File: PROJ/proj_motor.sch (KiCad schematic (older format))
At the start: 12 parts

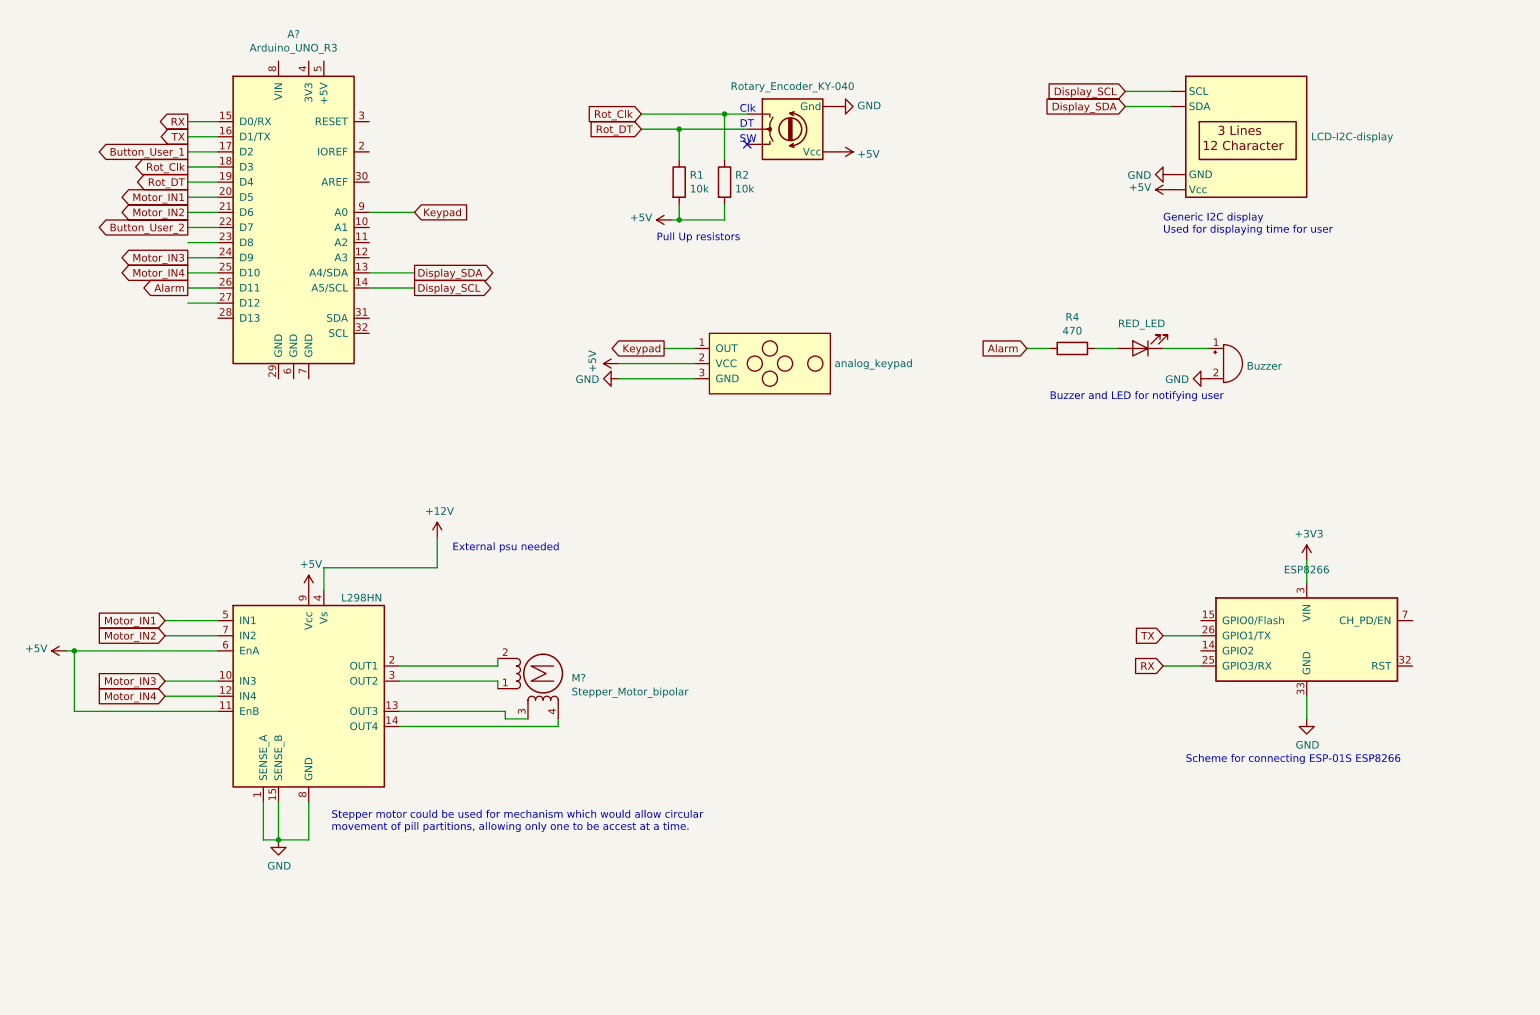
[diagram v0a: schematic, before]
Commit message: adding backup batery to proj
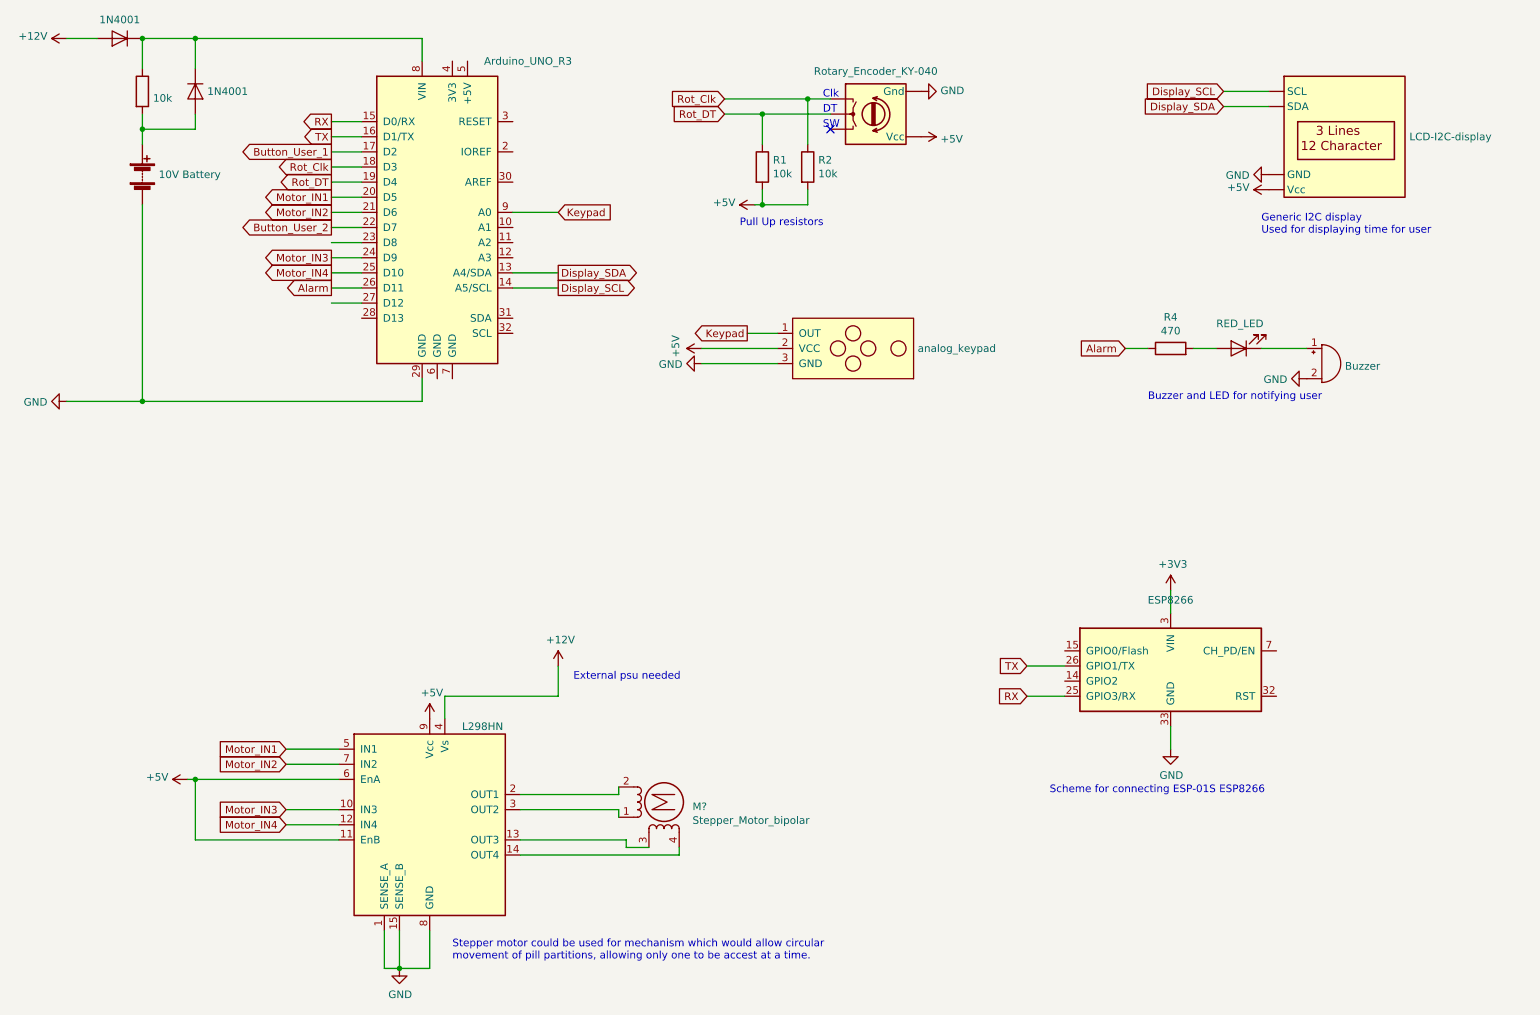
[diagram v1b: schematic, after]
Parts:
- added BT?: 10V Battery, symbol Device:Battery
- added D? (x2): 1N4001, Diode_THT:D_DO-41_SOD81_P10.16mm_Horizontal, symbol Diode:1N4001
- added R?: 10k, symbol Device:R
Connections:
- net +12V: now also D?.2 (A)
- net GND: now also A?.29 (GND), BT?.2 (-)
- net at A?.8 (VIN): now also D?.1 (K), D?.1 (K), R?.1
- new net: BT?.1 (+), D?.2 (A), R?.2
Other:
- moved on the sheet: M?, R1, R2, R4

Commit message: projV1_4
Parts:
- removed BZ?: Buzzer, symbol Device:Buzzer
- removed D?: RED_LED, symbol Device:LED
- removed R4: 470, symbol Device:R
- added LS?: Speaker, symbol Device:Speaker
- added SW?: SW_DIP_x01, symbol Switch:SW_DIP_x01
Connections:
- net +3V3: now also SW?.2
- net GND: now also LS?.2
- net Offline-online_switch: now reaches A?.11 (A2)
- net Offline-online_switch: now also SW?.1
- net Alarm renamed Speaker
- net Speaker: now also LS?.1
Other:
- note added: "Speaker for notyfing user"
- note added: "Switch for switching between offline and online mode"
- note removed: "Buzzer and LED for notifying user"
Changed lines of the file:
@@
 encoding utf-8
 Sheet 1 1
-Title "Pill helper V1.3 (motor approach)"
+Title "Pill helper V1.4 (motor approach)"
 Date "2020-12-27"
-Rev "1.3"
+Rev "1.4"
 Comp "FEL CVUT"
 Comment1 "First ideas about all potential functionalities of Pill helper using motor"
@@
 Pull Up resistors
 Text GLabel 2750 2550 0    50   Output ~ 0
-Alarm
-$Comp
-L Device:Buzzer BZ?
-U 1 1 5FDA69A7
-P 9300 3050
-F 0 "BZ?" H 9453 3079 50  0001 L CNN
-F 1 "Buzzer" H 9453 3033 50  0000 L CNN
-F 2 "" V 9275 3150 50  0001 C CNN
-F 3 "~" V 9275 3150 50  0001 C CNN
-	1    9300 3050
-	1    0    0    -1
-$EndComp
-Text GLabel 8000 2950 0    50   Input ~ 0
-Alarm
+Speaker
+Text GLabel 5200 3950 0    50   Input ~ 0
+Speaker
 $Comp
 L power:GND #PWR?
 U 1 1 5FDA6EF6
-P 9200 3150
-F 0 "#PWR?" H 9200 2900 50  0001 C CNN
-F 1 "GND" V 9205 3022 50  0000 R CNN
-F 2 "" H 9200 3150 50  0001 C CNN
-F 3 "" H 9200 3150 50  0001 C CNN
-	1    9200 3150
+P 5500 4050
+F 0 "#PWR?" H 5500 3800 50  0001 C CNN
+F 1 "GND" V 5505 3922 50  0000 R CNN
+F 2 "" H 5500 4050 50  0001 C CNN
+F 3 "" H 5500 4050 50  0001 C CNN
+	1    5500 4050
 	0    1    1    0
 $EndComp
@@
 Wire Wire Line
 	2750 2550 2950 2550
-Text Notes 8150 3300 0    50   ~ 0
-Buzzer and LED for notifying user
+Text Notes 4950 4300 0    50   ~ 0
+Speaker for notyfing user
 $Comp
 L Display_Character:EA_T123X-I2C U?
@@
 	0    1    1    0
 $EndComp
-$Comp
-L Device:LED D?
-U 1 1 5FDAF8D1
-P 8750 2950
-F 0 "D?" H 8741 3166 50  0001 C CNN
-F 1 "RED_LED" H 8742 2786 50  0000 C CNN
-F 2 "" H 8750 2950 50  0001 C CNN
-F 3 "~" H 8750 2950 50  0001 C CNN
-	1    8750 2950
-	-1   0    0    1
-$EndComp
 Wire Wire Line
 	2750 2250 2950 2250
 Wire Wire Line
 	2750 2650 2950 2650
-$Comp
-L Device:R R4
-U 1 1 5FDB61AB
-P 8300 2950
-F 0 "R4" V 8507 2950 50  0000 C CNN
-F 1 "470" V 8416 2950 50  0000 C CNN
-F 2 "" V 8230 2950 50  0001 C CNN
-F 3 "~" H 8300 2950 50  0001 C CNN
-	1    8300 2950
-	0    -1   -1   0
-$EndComp
-Wire Wire Line
-	8000 2950 8150 2950
-Wire Wire Line
-	8450 2950 8600 2950
 Text GLabel 2750 1450 0    50   Output ~ 0
 RX
@@
 $EndComp
 Wire Wire Line
-	8900 2950 9200 2950
+	5200 3950 5500 3950
 Wire Wire Line
 	4250 2050 3950 2050
@@
 	3350 3300 3350 3150
 Connection ~ 1500 3300
+Text GLabel 4250 2250 2    50   Input ~ 0
+Offline-online_switch
+Wire Wire Line
+	4250 2250 3950 2250
+Text GLabel 2100 3950 0    50   Output ~ 0
+Offline-online_switch
+$Comp
+L Switch:SW_DIP_x01 SW?
+U 1 1 6000BC5A
+P 2700 3950
+F 0 "SW?" H 2700 4217 50  0001 C CNN
+F 1 "SW_DIP_x01" H 2700 4125 50  0000 C CNN
+F 2 "" H 2700 3950 50  0001 C CNN
+F 3 "" H 2700 3950 50  0001 C CNN
+	1    2700 3950
+	1    0    0    -1
+$EndComp
+Wire Wire Line
+	2400 3950 2100 3950
+Wire Wire Line
+	3000 3950 3300 3950
+$Comp
+L power:+3V3 #PWR?
+U 1 1 60010456
+P 3300 3950
+F 0 "#PWR?" H 3300 3800 50  0001 C CNN
+F 1 "+3V3" V 3315 4078 50  0000 L CNN
+F 2 "" H 3300 3950 50  0001 C CNN
+F 3 "" H 3300 3950 50  0001 C CNN
+	1    3300 3950
+	0    1    1    0
+$EndComp
+Text Notes 1500 4250 0    50   ~ 0
+Switch for switching between offline and online mode
+$Comp
+L Device:Speaker LS?
+U 1 1 6001063D
+P 5700 3950
+F 0 "LS?" H 5870 3946 50  0001 L CNN
+F 1 "Speaker" H 5870 3900 50  0000 L CNN
+F 2 "" H 5700 3750 50  0001 C CNN
+F 3 "~" H 5690 3900 50  0001 C CNN
+	1    5700 3950
+	1    0    0    -1
+$EndComp
 $EndSCHEMATC
